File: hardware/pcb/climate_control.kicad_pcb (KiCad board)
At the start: 2 copper layers, 18 x 55 mm, 34 parts, among them J1 Switch, J2 BatteryIn, J3 USB_C, J4 HeatElement, J5 ICSP, Q2 NTR3C21NZ, U1 TP4056, U2 XB8089A, U3 ATmega328PB-AU, U4 TPS61230DRC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

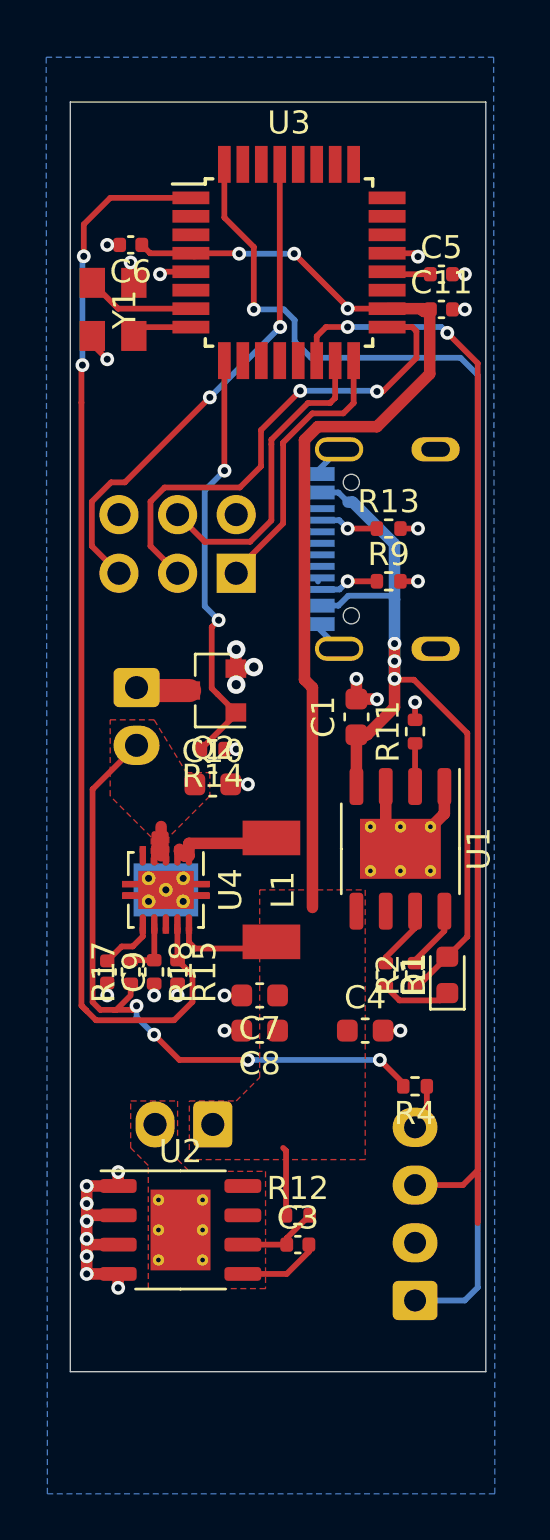
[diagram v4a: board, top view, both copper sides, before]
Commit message: Routing complete and added some silkscreen.
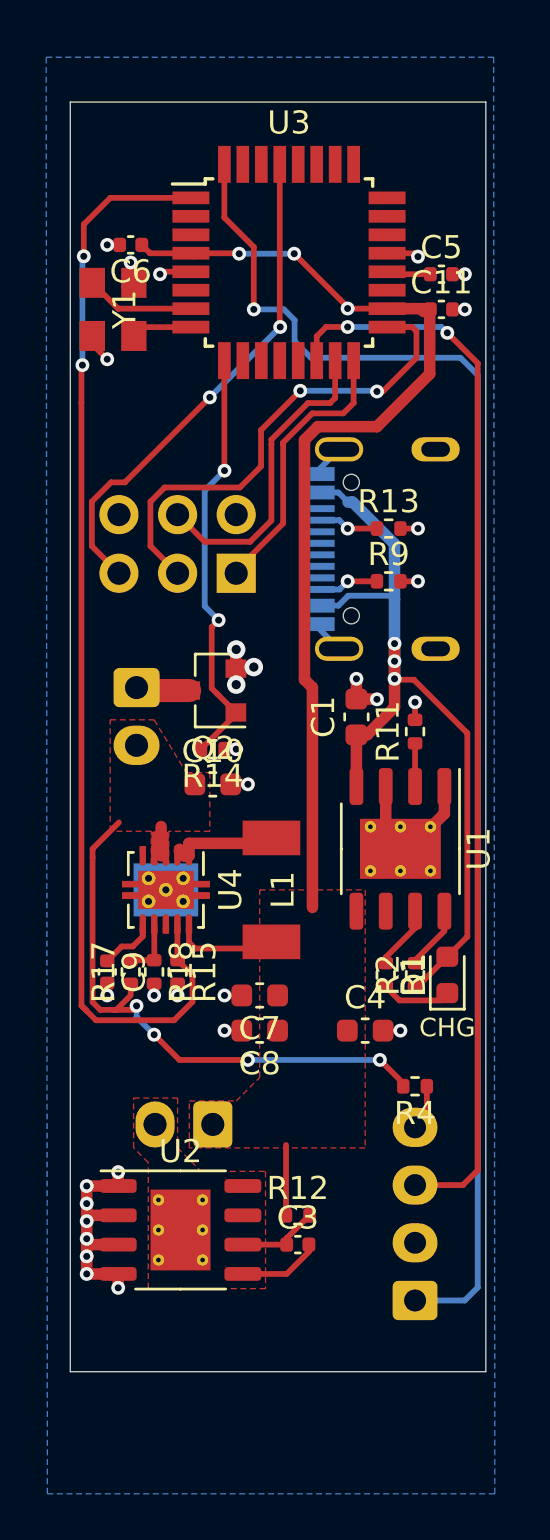
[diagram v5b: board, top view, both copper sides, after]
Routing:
- net +VSW: track 32.3 -> 28.7 mm
- net LED: track 49.1 -> 46.8 mm
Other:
- rule trace_min: 0.2 -> 0.15
- board text added: "CHG"
- board text added: "MISO|SCK |RST"
- board text removed: "MISO|SCK|RST"
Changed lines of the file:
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@@
   (general
     (thickness 1.6)
-    (drawings 14)
-    (tracks 326)
+    (drawings 15)
+    (tracks 325)
     (zones 0)
     (modules 34)
@@
   )
   (setup
-    (last_trace_width 0.5)
+    (last_trace_width 0.25)
     (user_trace_width 0.5)
     (user_trace_width 1)
@@
     (zone_clearance 0.508)
     (zone_45_only no)
-    (trace_min 0.2)
+    (trace_min 0.15)
     (via_size 0.8)
     (via_drill 0.4)
@@
       (net 43 "Net-(L1-Pad2)"))
   )
-  (gr_text MISO|SCK|RST (at 104.648 116.332) (layer B.SilkS)
+  (gr_text CHG (at 116.332 141.097) (layer F.SilkS)
+    (effects (font (size 0.8 0.8) (thickness 0.16)))
+  )
+  (gr_text "MISO|SCK |RST" (at 105.791 114.427) (layer B.SilkS)
     (effects (font (size 0.8 0.8) (thickness 0.16)) (justify mirror))
   )
-  (gr_text "     -|MOSI|GND\n" (at 105.664 114.808) (layer B.SilkS)
+  (gr_text "     -|MOSI|GND\n" (at 106.172 112.903) (layer B.SilkS)
     (effects (font (size 0.8 0.8) (thickness 0.16)) (justify mirror))
   )
@@
   (via (at 112.014 109.943997) (size 0.6) (drill 0.3) (layers F.Cu B.Cu) (net 4))
   (segment (start 112.020003 109.95) (end 112.014 109.943997) (width 0.25) (layer F.Cu) (net 4))
-  (segment (start 109.345 149.225) (end 109.345 146.429) (width 0.25) (layer F.Cu) (net 4))
-  (segment (start 109.345 146.429) (end 109.22 146.304) (width 0.25) (layer F.Cu) (net 4))
   (segment (start 115.316 109.982) (end 115.284 109.95) (width 0.25) (layer F.Cu) (net 4))
   (segment (start 115.598 109.982) (end 115.316 109.982) (width 0.25) (layer F.Cu) (net 4))
@@
   (segment (start 112.014 109.884) (end 112.014 109.943997) (width 0.25) (layer F.Cu) (net 4))
   (segment (start 109.699 107.569) (end 112.014 109.884) (width 0.25) (layer F.Cu) (net 4))
+  (segment (start 109.345 149.225) (end 109.347 146.177) (width 0.25) (layer F.Cu) (net 4))
   (segment (start 113.832 108.458) (end 113.724 108.35) (width 0.25) (layer F.Cu) (net 5))
   (segment (start 115.598 108.458) (end 113.832 108.458) (width 0.25) (layer F.Cu) (net 5))
@@
   (segment (start 102.22501 137.57899) (end 101.6 138.204) (width 0.25) (layer F.Cu) (net 6))
   (segment (start 102.70501 137.57899) (end 102.22501 137.57899) (width 0.25) (layer F.Cu) (net 6))
-  (segment (start 101.299999 140.325001) (end 101.900001 140.325001) (width 0.25) (layer F.Cu) (net 7))
-  (segment (start 100.96499 139.989992) (end 101.299999 140.325001) (width 0.25) (layer F.Cu) (net 7))
-  (segment (start 100.96499 130.77001) (end 100.96499 139.989992) (width 0.25) (layer F.Cu) (net 7))
   (segment (start 102.616 139.609002) (end 102.616 139.194) (width 0.25) (layer F.Cu) (net 7))
-  (segment (start 102.87 128.865) (end 100.96499 130.77001) (width 0.25) (layer F.Cu) (net 7))
-  (segment (start 101.900001 140.325001) (end 101.990999 140.325001) (width 0.25) (layer F.Cu) (net 7))
   (segment (start 101.990999 140.325001) (end 102.616 139.7) (width 0.25) (layer F.Cu) (net 7))
   (segment (start 103.64 133.653) (end 103.64 132.707) (width 0.25) (layer F.Cu) (net 7))
@@
   (segment (start 114.425 143.508) (end 113.411 142.494) (width 0.25) (layer F.Cu) (net 7))
   (segment (start 114.425 143.637) (end 114.425 143.508) (width 0.25) (layer F.Cu) (net 7))
+  (segment (start 101.900001 140.325001) (end 101.990999 140.325001) (width 0.25) (layer F.Cu) (net 7))
+  (segment (start 101.299999 140.325001) (end 101.900001 140.325001) (width 0.25) (layer F.Cu) (net 7))
+  (segment (start 100.965 133.731) (end 100.96499 139.989992) (width 0.25) (layer F.Cu) (net 7))
+  (segment (start 100.96499 139.989992) (end 101.299999 140.325001) (width 0.25) (layer F.Cu) (net 7))
+  (segment (start 100.965 133.731) (end 100.965 133.35) (width 0.25) (layer F.Cu) (net 7))
+  (segment (start 100.965 133.35) (end 102.108 132.207) (width 0.25) (layer F.Cu) (net 7))
   (segment (start 114.935 138.176506) (end 114.935 138.301) (width 0.25) (layer F.Cu) (net 8))
   (segment (start 116.205 136.906506) (end 114.935 138.176506) (width 0.25) (layer F.Cu) (net 8))
@@
   (segment (start 117.007 147.915) (end 114.935 147.915) (width 0.25) (layer F.Cu) (net 13))
   (segment (start 117.64999 147.27201) (end 117.007 147.915) (width 0.25) (layer F.Cu) (net 13))
-  (segment (start 116.332 110.998) (end 117.64999 112.31599) (width 0.25) (layer F.Cu) (net 13))
-  (segment (start 117.64999 112.31599) (end 117.64999 149.55801) (width 0.25) (layer F.Cu) (net 13))
   (via (at 116.332 110.998) (size 0.6) (drill 0.3) (layers F.Cu B.Cu) (net 13))
   (segment (start 112.014 110.744) (end 116.078 110.744) (width 0.25) (layer B.Cu) (net 13))
   (segment (start 116.078 110.744) (end 116.332 110.998) (width 0.25) (layer B.Cu) (net 13))
+  (segment (start 117.64999 112.31599) (end 117.64999 147.27201) (width 0.25) (layer F.Cu) (net 13))
+  (segment (start 116.332 110.998) (end 117.64999 112.31599) (width 0.25) (layer F.Cu) (net 13))
   (segment (start 114.935 130.65) (end 114.935 128.78) (width 0.25) (layer F.Cu) (net 14))
   (segment (start 106.380001 126.650001) (end 107.172 127.442) (width 0.25) (layer F.Cu) (net 16))
@@
   (segment (start 110.729 116.959) (end 111.644 116.044) (width 0.25) (layer B.Cu) (net 50))
   (segment (start 110.729 123.769) (end 111.644 124.684) (width 0.25) (layer B.Cu) (net 50))
-  (segment (start 110.729 121.614) (end 110.729 121.769) (width 0.25) (layer B.Cu) (net 49))
   (via (at 115.062 121.761) (size 0.6) (drill 0.3) (layers F.Cu B.Cu) (net 50))
   (segment (start 114.302 121.761) (end 115.062 121.761) (width 0.25) (layer F.Cu) (net 50))
@@
     (polygon
       (pts
-        (xy 112.776 146.812) (xy 105.156 146.812) (xy 105.156 144.272) (xy 107.188 144.272) (xy 108.204 143.256)
+        (xy 112.776 146.304) (xy 105.156 146.304) (xy 105.156 144.272) (xy 107.188 144.272) (xy 108.204 143.256)
         (xy 108.204 135.128) (xy 112.776 135.128)
       )
@@
     (polygon
       (pts
-        (xy 104.648 146.812) (xy 105.156 147.32) (xy 108.458 147.32) (xy 108.458 152.4) (xy 103.378 152.4)
-        (xy 103.378 147.066) (xy 102.616 146.304) (xy 102.616 144.272) (xy 104.648 144.272)
+        (xy 104.648 146.304) (xy 105.664 147.32) (xy 108.458 147.32) (xy 108.458 152.4) (xy 103.378 152.4)
+        (xy 103.378 146.939) (xy 102.743 146.304) (xy 102.743 144.145) (xy 104.648 144.145)
       )
     )
@@
     (polygon
       (pts
-        (xy 105.029 130.048) (xy 106.045 130.048) (xy 106.045 131.064) (xy 104.267 132.842) (xy 104.267 133.985)
-        (xy 103.505 133.985) (xy 103.505 132.842) (xy 101.727 131.064) (xy 101.727 130.048) (xy 101.727 127.762)
+        (xy 105.029 130.048) (xy 106.045 130.048) (xy 106.045 132.588) (xy 104.267 132.588) (xy 104.267 133.985)
+        (xy 103.505 133.985) (xy 103.505 132.588) (xy 101.727 132.588) (xy 101.727 130.048) (xy 101.727 127.762)
         (xy 103.632 127.762)
       )

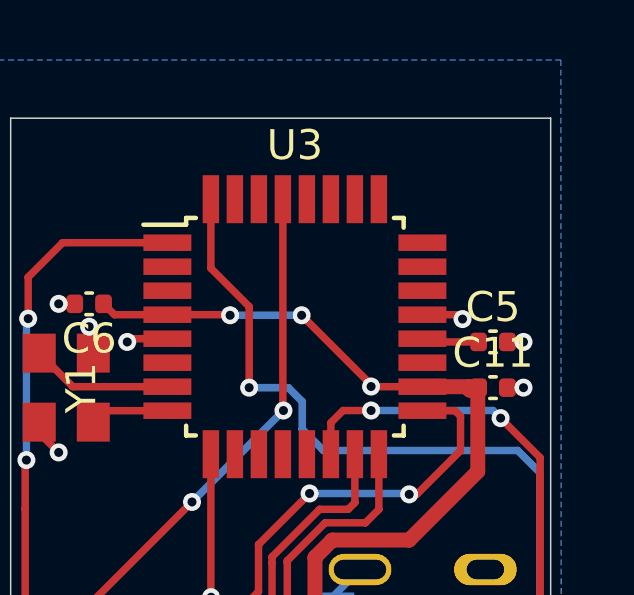
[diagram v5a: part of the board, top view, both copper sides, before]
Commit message: Added battery divider to MCU.
A voltage divider from the battery is now connected to the MCU.
The divider is designed to work with the internal voltage reference (1V1).
With the resistor values, a battery voltage of 5 V will be 1.15 at MCU.
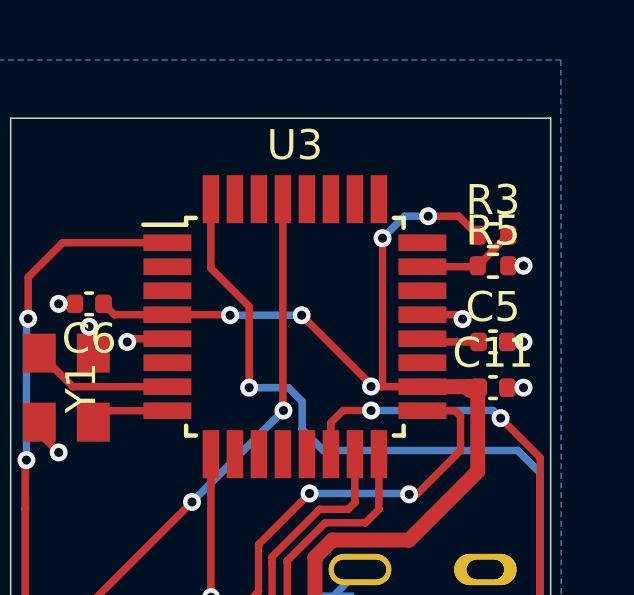
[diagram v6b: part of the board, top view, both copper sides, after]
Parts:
- added R3: 100k, Resistor_SMD:R_0402_1005Metric, F.Cu at (116.1, 104.9)
- added R5: 30k, Resistor_SMD:R_0402_1005Metric, F.Cu at (116.1, 105.9)
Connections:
- U3 pad 23: A0 -> BAT
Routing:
- net +BATT: track 51.5 -> 60.2 mm, vias 3 -> 5
- net BAT: track 0.00 -> 3.30 mm
- net GND: track 43.4 -> 43.9 mm, vias 31 -> 32

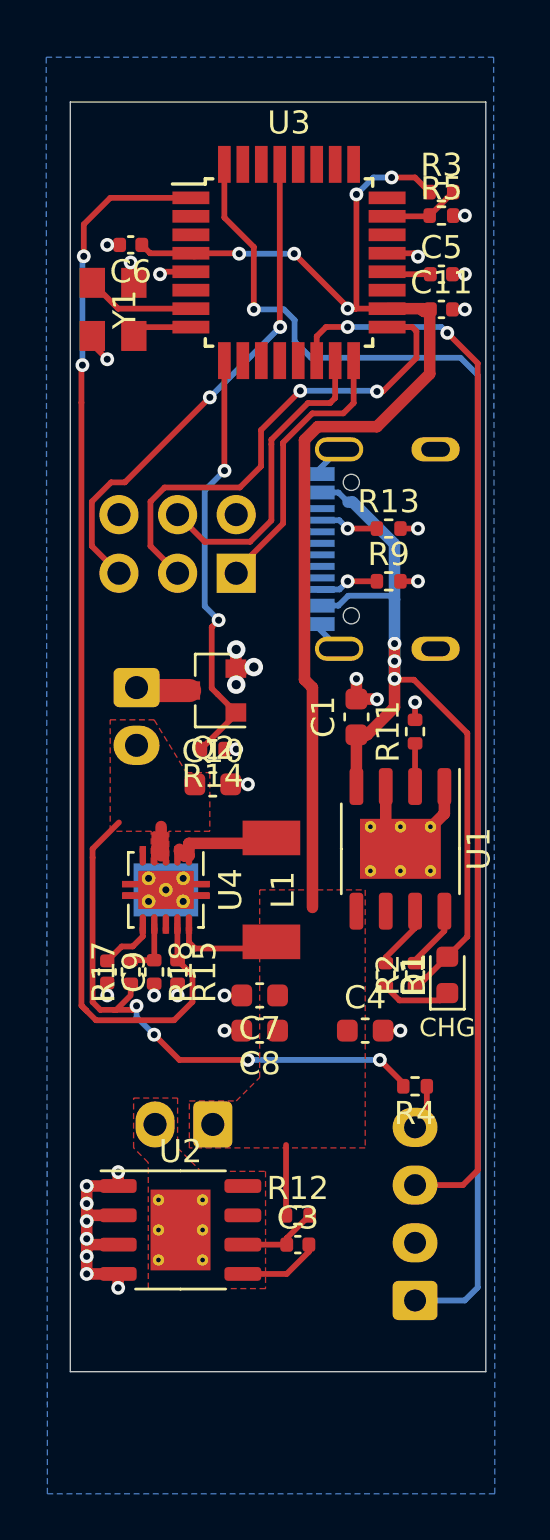
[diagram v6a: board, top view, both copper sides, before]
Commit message: Removed crystal.
The ATMega does not need an external crystal. Now removed.
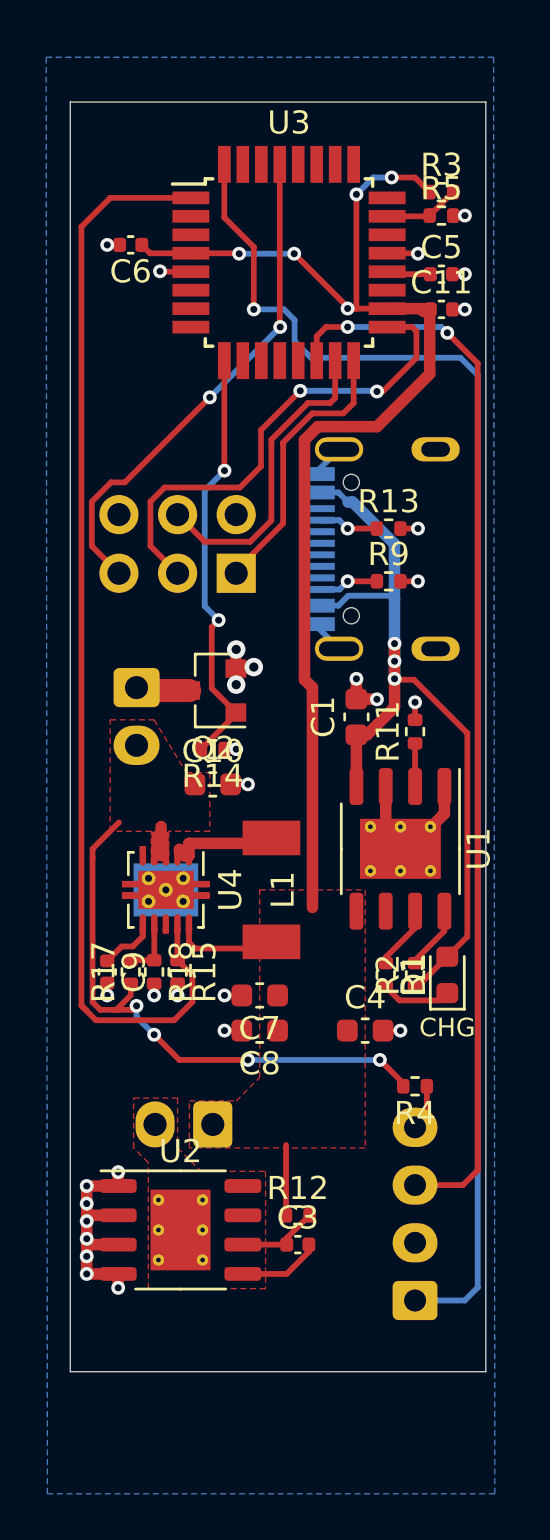
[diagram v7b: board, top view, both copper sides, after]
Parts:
- removed Y1: 8MHz, climate_control:ECX-32
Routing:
- net Net-(U3-Pad7): track 4.73 -> 0.00 mm
- net Net-(U3-Pad8): track 2.63 -> 0.00 mm
- net GND: track 43.9 -> 41.6 mm, vias 32 -> 30
- net BOOST_EN: vias 2 -> 0

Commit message: Final first revision ordered.
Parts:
- moved D1 11.2 mm to (116.5, 127.6)
- moved C10 1.14 mm to (107.3, 130.6)
- moved J4 1.14 mm to (104.0, 126.4)
- moved Q2 1.14 mm to (107.3, 126.5)
- moved R14 1.14 mm to (107.3, 129.0)
- moved J1 1.02 mm to (113.9, 152.9)
- moved J2 0.76 mm to (106.9, 145.3)
- moved C6 0.38 mm to (102.6, 107.6)
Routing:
- net Net-(D1-Pad1): track 3.04 -> 14.5 mm
- net +5V: track 36.9 -> 39.0 mm, vias 3 -> 5
- net +VSW: track 28.7 -> 30.5 mm
- net SWITCH: track 60.7 -> 62.0 mm
- net Net-(J1-Pad4): track 1.99 -> 3.01 mm
- net LED: track 46.8 -> 47.8 mm
- net HEATER_PWM: track 18.6 -> 19.3 mm
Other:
- board text added: "Climate control 2021 - Rev 1"
- board text removed: "CHG"
